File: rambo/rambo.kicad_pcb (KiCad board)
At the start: 2 copper layers, 39 parts, among them J1 Barrel_Jack, J2 Conn_02x25_Odd_Even, Q1 2N7000, SW1 SW_DIP_x04, U1 74LS139, U10 74HCT04, U11 74LS245, U12 74HCT00, U13 74LS85, U14 74HCT02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

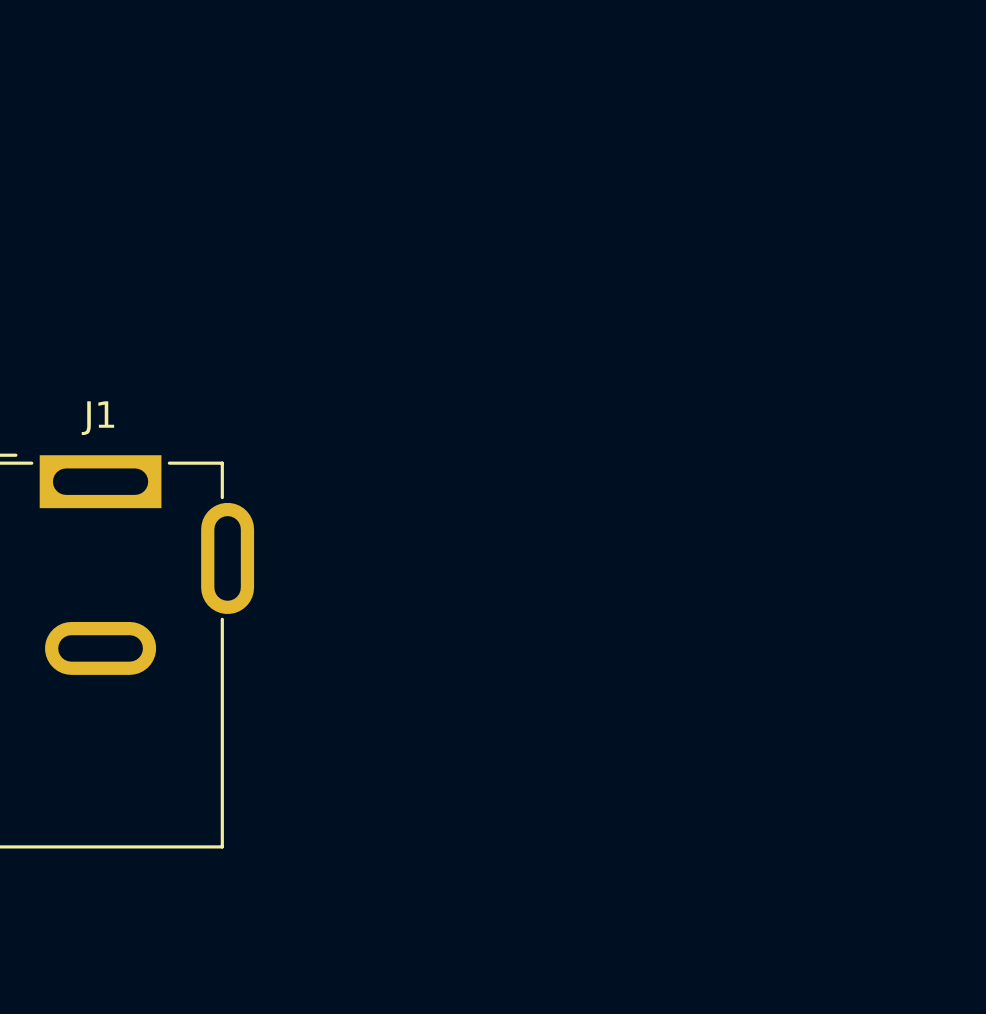
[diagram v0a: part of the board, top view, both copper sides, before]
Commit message: added usb b for power
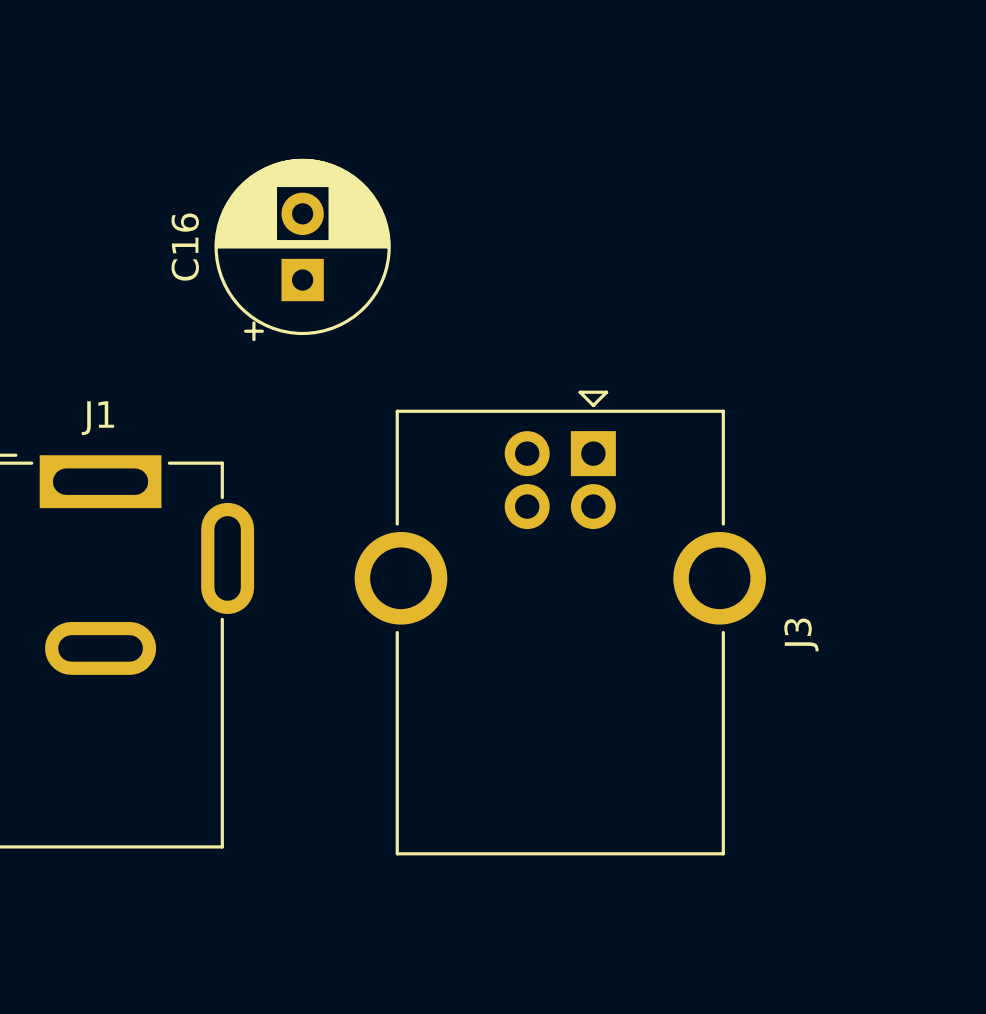
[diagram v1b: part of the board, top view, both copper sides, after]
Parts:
- added C16: 33uF, Capacitor_THT:CP_Radial_D6.3mm_P2.50mm, F.Cu at (44.5, 144.1)
- added J3: USB_B, Connector_USB:USB_B_OST_USB-B1HSxx_Horizontal, F.Cu at (55.4, 150.7)

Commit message: first layout done
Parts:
- removed U16: 74LS139, Package_DIP:DIP-16_W7.62mm
- removed U17: 74HCT04, Package_DIP:DIP-14_W7.62mm
- removed U18: 74HCT00, Package_DIP:DIP-14_W7.62mm
- removed U19: 74HCT02, Package_DIP:DIP-14_W7.62mm
- added G***: LOGO, Evan's misc parts:Evan Logo, F.Cu at (177.3, 123.1)
- added G***: LOGO, Evan's misc parts:OSHW gear, F.Cu at (234.3, 141.5)
- added h1: MountingHole_3.2mm_M3, MountingHole:MountingHole_3.2mm_M3, F.Cu at (122.9, 69.6)
- added h2: MountingHole_3.2mm_M3, MountingHole:MountingHole_3.2mm_M3, F.Cu at (246.6, 69.6)
- added h3: MountingHole_3.2mm_M3, MountingHole:MountingHole_3.2mm_M3, F.Cu at (246.6, 143.8)
- added h4: MountingHole_3.2mm_M3, MountingHole:MountingHole_3.2mm_M3, F.Cu at (122.9, 143.8)
- J1: value Barrel_Jack -> Barrel_Jack_Switch
- U15: value 74HCT02 -> 74LS139; footprint Package_DIP:DIP-14_W7.62mm -> Package_DIP:DIP-16_W7.62mm
- moved C10 353.2 mm to (222.2, 122.0), turned to -90 degrees
- moved C13 341.7 mm to (219.7, 110.5), turned to -90 degrees
- moved U8 334.4 mm to (132.6, 145.3), turned to 90 degrees
- moved C12 317.6 mm to (194.8, 108.0), turned to -90 degrees
- moved C11 310.7 mm to (214.6, 79.4), turned to -90 degrees
- moved C14 308.8 mm to (189.9, 94.9), turned to -90 degrees
- moved U9 308.4 mm to (132.6, 126.8), turned to 90 degrees
- moved C8 288.3 mm to (129.4, 136.4), turned to -90 degrees
- moved C7 280.3 mm to (156.7, 97.3), turned to -90 degrees
- moved U10 279.7 mm to (225.4, 127.0), turned to 90 degrees
- moved C9 276.9 mm to (129.4, 117.9), turned to -90 degrees
- moved C5 268.2 mm to (156.7, 85.9), turned to -90 degrees
- moved U2 263.4 mm to (188.0, 79.5), turned to 90 degrees
- moved U1 261.1 mm to (190.5, 90.9), turned to 90 degrees
- moved U12 260.8 mm to (198.1, 115.6), turned to 90 degrees
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- renumbered J3 to J2, J2 to J3
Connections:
- J1 pad 3: (no net) -> GND
- SW1 pad 1: GND -> Net-(RN1-Pad2)
- SW1 pad 2: GND -> Net-(RN1-Pad3)
- SW1 pad 3: GND -> Net-(RN1-Pad4)
- SW1 pad 4: GND -> Net-(RN1-Pad5)
- SW1 pad 5: Net-(RN1-Pad5) -> GND
- SW1 pad 6: Net-(RN1-Pad4) -> GND
- SW1 pad 7: Net-(RN1-Pad3) -> GND
- SW1 pad 8: Net-(RN1-Pad2) -> GND
- U10 pad 10: (no net) -> unconnected-(U10-Pad10)
- U10 pad 11: (no net) -> unconnected-(U10-Pad11)
- U10 pad 12: (no net) -> unconnected-(U10-Pad12)
- U10 pad 13: (no net) -> unconnected-(U10-Pad13)
- U10 pad 14: (no net) -> +5V
- U10 pad 7: (no net) -> GND
- U10 pad 8: (no net) -> unconnected-(U10-Pad8)
- U10 pad 9: (no net) -> unconnected-(U10-Pad9)
- U12 pad 1: Net-(U10-Pad2) -> Net-(U10-Pad4)
- U12 pad 10: (no net) -> unconnected-(U12-Pad10)
- U12 pad 11: (no net) -> unconnected-(U12-Pad11)
- U12 pad 12: (no net) -> unconnected-(U12-Pad12)
- U12 pad 13: (no net) -> unconnected-(U12-Pad13)
- U12 pad 14: (no net) -> +5V
- U12 pad 3: /~{READ} -> /~{WRITE}
- U12 pad 4: Net-(U10-Pad4) -> Net-(U10-Pad2)
- U12 pad 6: /~{WRITE} -> /~{READ}
- U12 pad 7: (no net) -> GND
- U12 pad 8: (no net) -> unconnected-(U12-Pad8)
- U12 pad 9: (no net) -> unconnected-(U12-Pad9)
- U14 pad 1: Net-(U14-Pad1) -> /ACLK
- U14 pad 10: (no net) -> Net-(U14-Pad10)
- U14 pad 11: /XA3 -> /~{RAMRD}
- U14 pad 12: /XA2 -> /~{CKASITRD}
- U14 pad 13: /EXTRAADDR -> Net-(U14-Pad13)
- U14 pad 14: (no net) -> +5V
- U14 pad 2: /~{RAMRD} -> Net-(U14-Pad13)
- U14 pad 3: /~{CKASITRD} -> Net-(U14-Pad10)
- U14 pad 4: Net-(U14-Pad4) -> /EXTRAADDR
- U14 pad 5: /~{RAMWR} -> /XA3
- U14 pad 6: /~{CKASITWR} -> /XA2
- U14 pad 7: (no net) -> GND
- U14 pad 8: (no net) -> /~{RAMWR}
- U14 pad 9: (no net) -> /~{CKASITWR}
- U15 pad 1: (no net) -> GND
- U15 pad 10: /ACLK -> unconnected-(U15-Pad10)
- U15 pad 11: (no net) -> unconnected-(U15-Pad11)
- U15 pad 12: (no net) -> unconnected-(U15-Pad12)
- U15 pad 13: (no net) -> unconnected-(U15-Pad13)
- U15 pad 14: (no net) -> unconnected-(U15-Pad14)
- U15 pad 2: (no net) -> /AR19
- U15 pad 3: (no net) -> /AR20
- U15 pad 4: (no net) -> Net-(U15-Pad4)
- U15 pad 5: (no net) -> Net-(U15-Pad5)
- U15 pad 6: (no net) -> unconnected-(U15-Pad6)
- U15 pad 7: (no net) -> unconnected-(U15-Pad7)
- U15 pad 8: Net-(U14-Pad1) -> GND
- U15 pad 9: Net-(U14-Pad4) -> unconnected-(U15-Pad9)
- U2 pad 12: /ADR20 -> /AR20
- U8 pad 22: Net-(U16-Pad5) -> Net-(U15-Pad5)
- U9 pad 22: Net-(U16-Pad4) -> Net-(U15-Pad4)
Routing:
- net +5V: track 0.00 -> 430.0 mm, vias 0 -> 19
- net /D5: track 0.00 -> 207.7 mm, vias 0 -> 4
- net /D4: track 0.00 -> 206.3 mm, vias 0 -> 4
- net /D6: track 0.00 -> 172.7 mm, vias 0 -> 3
- net /D7: track 0.00 -> 166.5 mm, vias 0 -> 2
- net /D1: track 0.00 -> 150.8 mm, vias 0 -> 6
- net /D0: track 0.00 -> 142.2 mm, vias 0 -> 1
- net /D2: track 0.00 -> 140.5 mm, vias 0 -> 3
- net /AR16: track 0.00 -> 139.2 mm, vias 0 -> 3
- net /AR18: track 0.00 -> 137.0 mm, vias 0 -> 3
- net /AR7: track 0.00 -> 131.7 mm, vias 0 -> 4
- net /D3: track 0.00 -> 128.9 mm, vias 0 -> 3
- net /AR6: track 0.00 -> 126.7 mm, vias 0 -> 4
- net /~{RAMWR}: track 0.00 -> 119.0 mm, vias 0 -> 2
- net /AR17: track 0.00 -> 116.0 mm, vias 0 -> 3
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- added copper zone on B.Cu, net GND
- added copper zone on F.Cu, net GND
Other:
- board outline added: 130.9 x 81.3 mm
- board text added: "1"
- board text added: "5V in"
- board text added: "A4"
- board text added: "A5"
- board text added: "A6"
- board text added: "A7"
- board text added: "Address range select"
- board text added: "Designed by: Frank Palazzolo Evan Allen"
- board text added: "TRS-80 Model 3 high speed RAM board"
- board text added: "TRS80 model 3 parallel interface"
- board text added: "abzman2k.wordpress.com"
- board text added: "https://github.com/palazzol/TRS80_3D"
- board text added: "or JEDEC 512Kx8 SRAM"

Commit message: fixed erc and drc
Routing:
- net /~{AREGLWR}: track 80.0 -> 79.2 mm
- net /AR2: track 61.9 -> 61.3 mm
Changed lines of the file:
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@@
   (via (at 172.593 123.825) (size 0.8) (drill 0.4) (layers "F.Cu" "B.Cu") (net 26))
   (segment (start 154.323489 144.168489) (end 154.323489 128.378511) (width 0.25) (layer "B.Cu") (net 26))
-  (segment (start 172.503489 115.988489) (end 172.503489 116.593489) (width 0.25) (layer "B.Cu") (net 26))
   (segment (start 172.503489 123.735489) (end 172.593 123.825) (width 0.25) (layer "B.Cu") (net 26))
   (segment (start 155.448 127.254) (end 155.448 126.751) (width 0.25) (layer "B.Cu") (net 26))
@@
   (segment (start 243.961621 85.211621) (end 243.961621 81.403057) (width 0.25) (layer "F.Cu") (net 42))
   (segment (start 242.334644 79.77608) (end 231.648 79.77608) (width 0.25) (layer "F.Cu") (net 42))
-  (segment (start 243.512101 81.589255) (end 243.512101 87.302101) (width 0.25) (layer "F.Cu") (net 43))
   (segment (start 242.148446 80.2256) (end 243.512101 81.589255) (width 0.25) (layer "F.Cu") (net 43))
   (segment (start 243.512101 87.302101) (end 245.745 89.535) (width 0.25) (layer "F.Cu") (net 43))
+  (segment (start 243.512101 81.589255) (end 243.512101 87.302101) (width 0.25) (layer "F.Cu") (net 43))
   (segment (start 233.05 84.445) (end 233.05 81.1096) (width 0.25) (layer "F.Cu") (net 43))
   (segment (start 233.05 81.1096) (end 233.934 80.2256) (width 0.25) (layer "F.Cu") (net 43))
@@
   (segment (start 171.323 93.427) (end 171.323 89.535) (width 0.25) (layer "B.Cu") (net 58))
   (segment (start 171.323 89.535) (end 171.323 86.995) (width 0.25) (layer "B.Cu") (net 58))
-  (segment (start 171.323 89.535) (end 171.323 88.773) (width 0.25) (layer "B.Cu") (net 58))
   (segment (start 171.323 86.995) (end 172.593 85.725) (width 0.25) (layer "B.Cu") (net 58))
   (segment (start 172.608 94.712) (end 171.323 93.427) (width 0.25) (layer "B.Cu") (net 58))
